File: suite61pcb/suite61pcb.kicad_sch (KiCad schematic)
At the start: 79 parts, among them J1 FFC_Receiver, J2 Joystick_FFC, J3 Battery JST, J4 OLED, SW1 MX_SW_HS, SW10 MX_SW_HS, SW11 MX_SW_HS, SW12 MX_SW_HS, SW13 MX_SW_HS, SW14 MX_SW_HS, SW15 MX_SW_HS, SW16 MX_SW_HS, SW17 MX_SW_HS, SW18 MX_SW_HS, SW19 MX_SW_HS, SW2 MX_SW_HS, SW20 MX_SW_HS, SW21 MX_SW_HS, SW22 MX_SW_HS, SW23 MX_SW_HS, SW24 MX_SW_HS, SW25 MX_SW_HS, SW26 MX_SW_HS, SW27 MX_SW_HS, SW28 MX_SW_HS, SW29 RotaryEncoder_Switch, SW3 MX_SW_HS, SW30 Reset_Button, SW4 MX_SW_HS, SW5 MX_SW_HS, SW6 MX_SW_HS, SW7 MX_SW_HS, SW8 MX_SW_HS, SW9 MX_SW_HS, U1 nice_nano

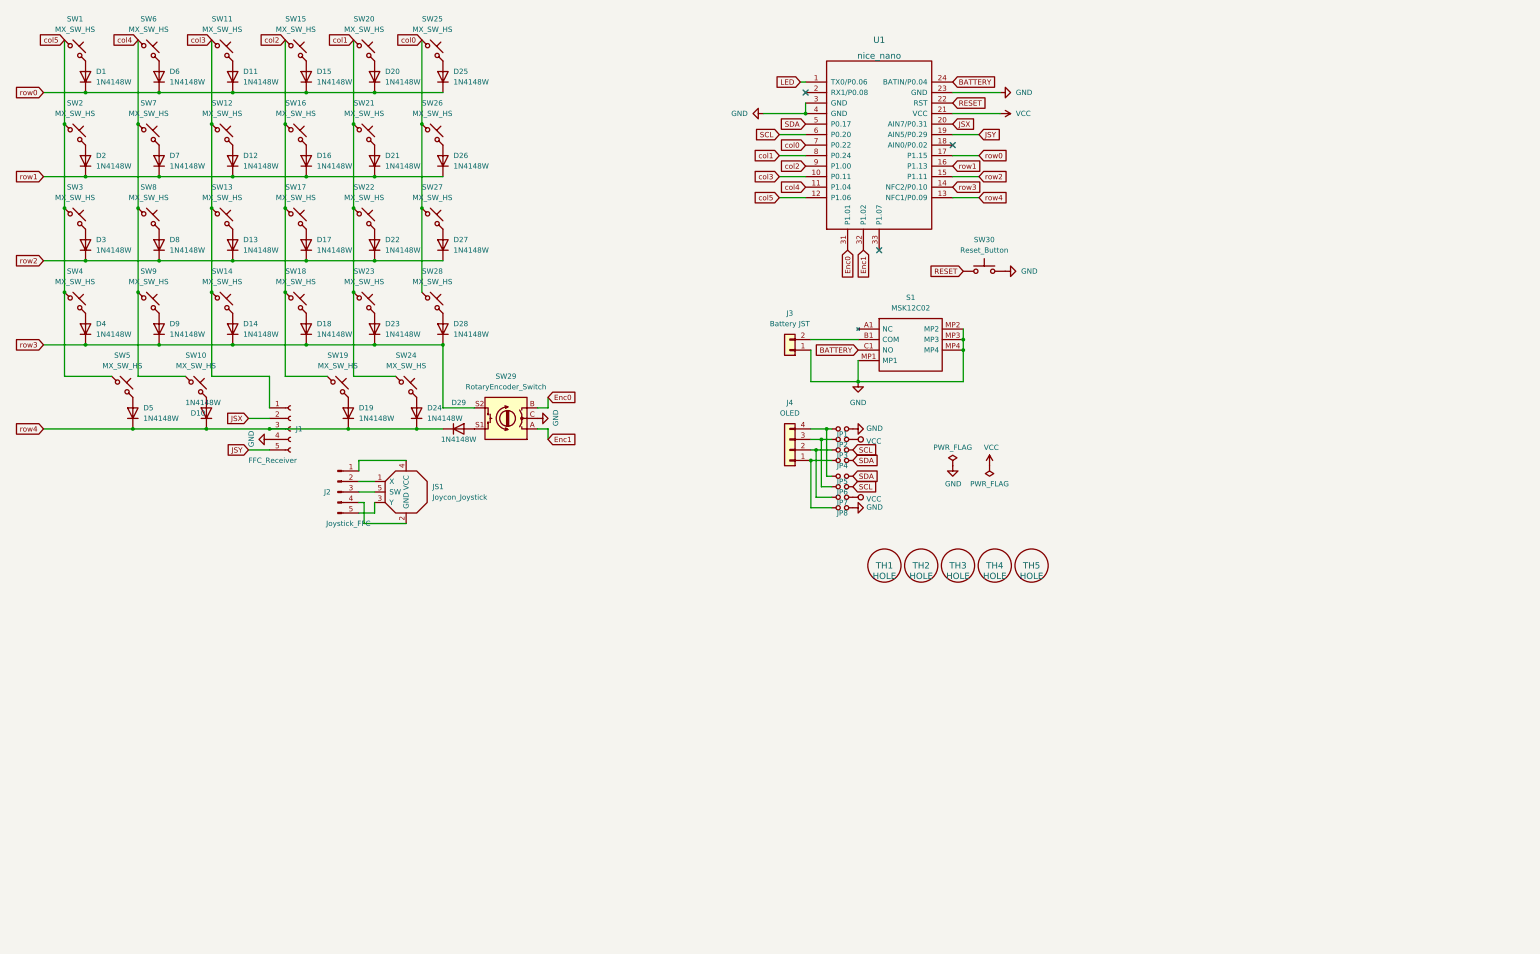
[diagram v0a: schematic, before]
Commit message: Update matrix to 6x6
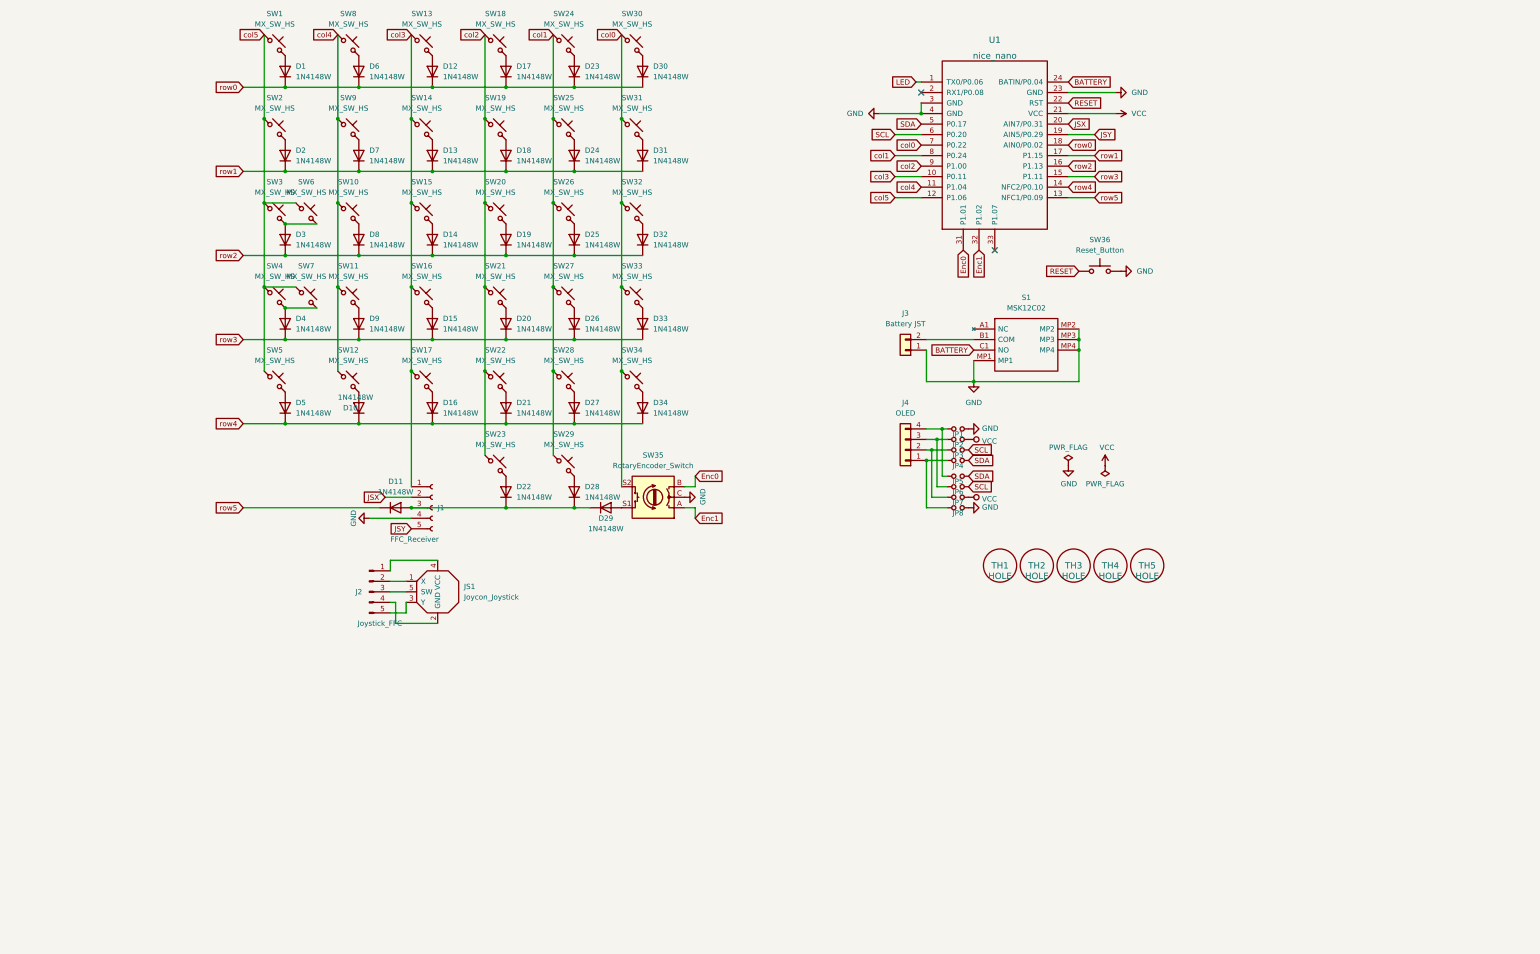
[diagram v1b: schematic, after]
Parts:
- added D11, D16, D22, D28, D34: 1N4148W, Diode_SMD:D_SOD-123, symbol Diode:1N4148W
- added SW17, SW23, SW29, SW34, SW6, SW7: MX_SW_HS, marbastlib-mx:SW_MX_HS_1u, symbol marbastlib-mx:MX_SW_HS
- renumbered D11 to D12, D12 to D13, D13 to D14, D14 to D15, D15 to D17, D16 to D18, D17 to D19, D18 to D20, D19 to D21, D20 to D23, D21 to D24, D22 to D25, D23 to D26, D24 to D27, D25 to D30, D26 to D31, D27 to D32, D28 to D33, SW8 to SW10, SW9 to SW11, SW10 to SW12, SW11 to SW13, SW12 to SW14, SW13 to SW15, SW14 to SW16, SW15 to SW18, SW16 to SW19, SW17 to SW20, SW18 to SW21, SW19 to SW22, SW20 to SW24, SW21 to SW25, SW22 to SW26, SW23 to SW27, SW24 to SW28, SW25 to SW30, SW26 to SW31, SW27 to SW32, SW28 to SW33, SW29 to SW35, SW30 to SW36, SW6 to SW8, SW7 to SW9
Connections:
- net col0: now also SW35.S2, SW34.1
- net col1: now also SW29.1
- net col2: now also SW23.1
- net col3: now also SW17.1
- net col5: now also SW6.1, SW7.1
- net row0: now also U1.18 (AIN0/P0.02); no longer U1.17 (P1.15)
- net row1: now also U1.17 (P1.15); no longer U1.16 (P1.13)
- net row2: now also U1.16 (P1.13); no longer U1.15 (P1.11)
- net row3: now also U1.15 (P1.11); no longer SW35.S2, U1.14 (NFC2/P0.10)
- net row4: now also U1.14 (NFC2/P0.10), D16.1 (K), D34.1 (K); no longer D29.1 (K), J1.3 (Pin_3), U1.13 (NFC1/P0.09)
- net at D3.2 (A), SW3.2: now also SW6.2
- net at D4.2 (A), SW4.2: now also SW7.2
- new net: D11.2 (A), D22.1 (K), D28.1 (K), D29.1 (K), J1.3 (Pin_3)
- new net: D34.2 (A), SW34.2
- new net: D16.2 (A), SW17.2
- new net: D28.2 (A), SW29.2
- new net: D22.2 (A), SW23.2
- new net row5: D11.1 (K), U1.13 (NFC1/P0.09)
- no-connect marks 3 -> 2
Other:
- moved on the sheet: D1, D10, D12, D13, D14, D15, D17, D18, D19, D2, D20, D21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

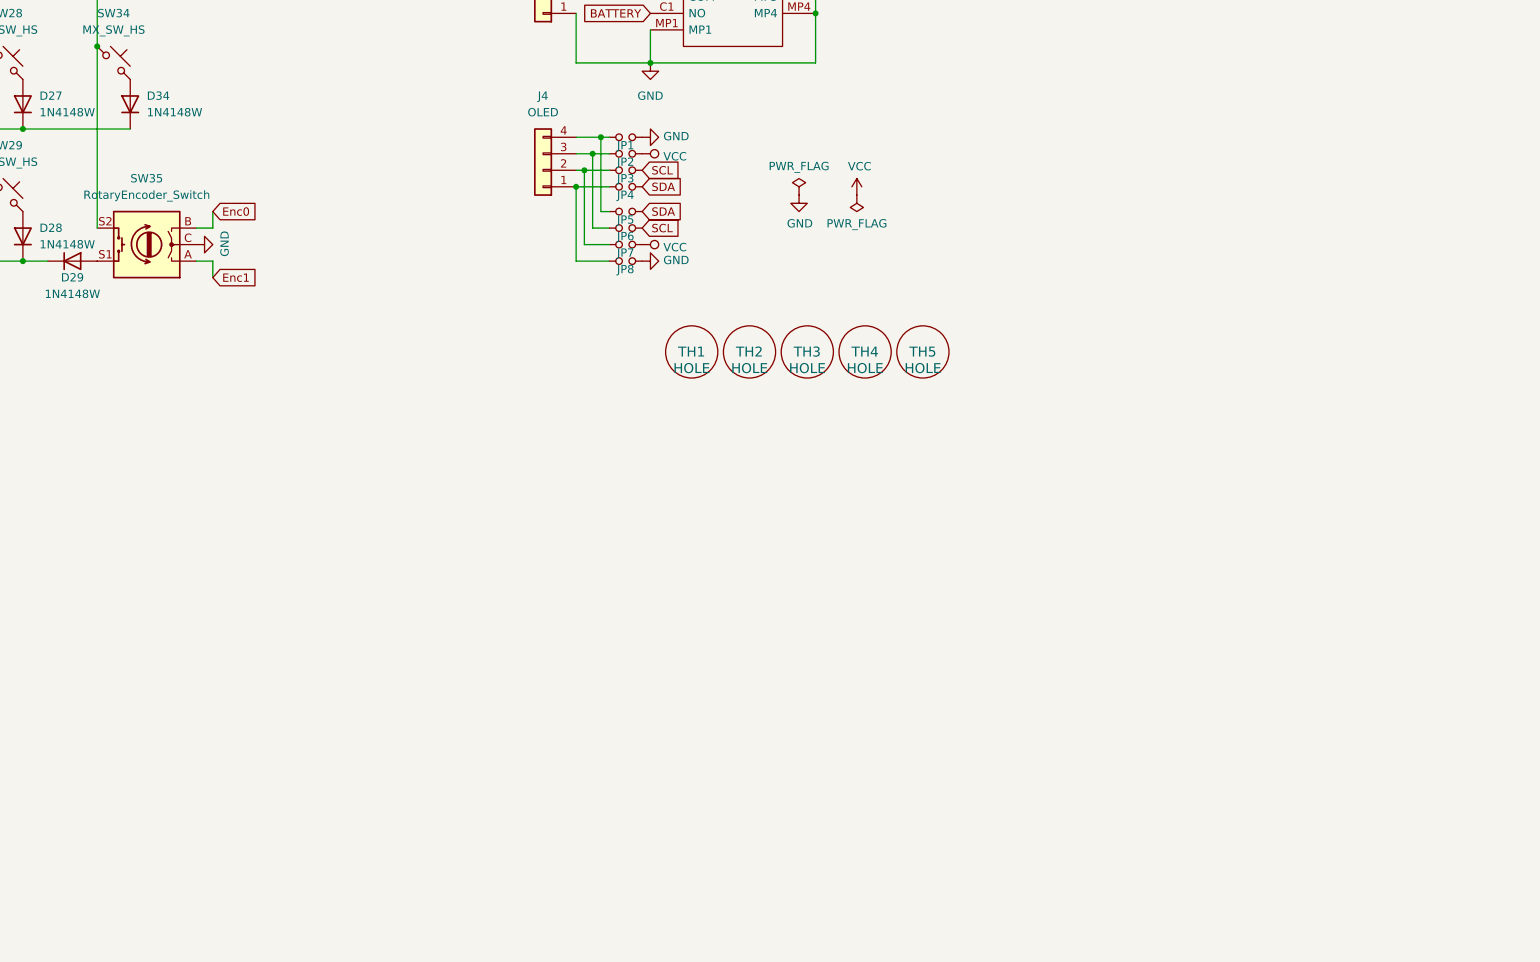
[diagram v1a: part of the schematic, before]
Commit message: create led underglow schematic, upload shield matrix KLE json
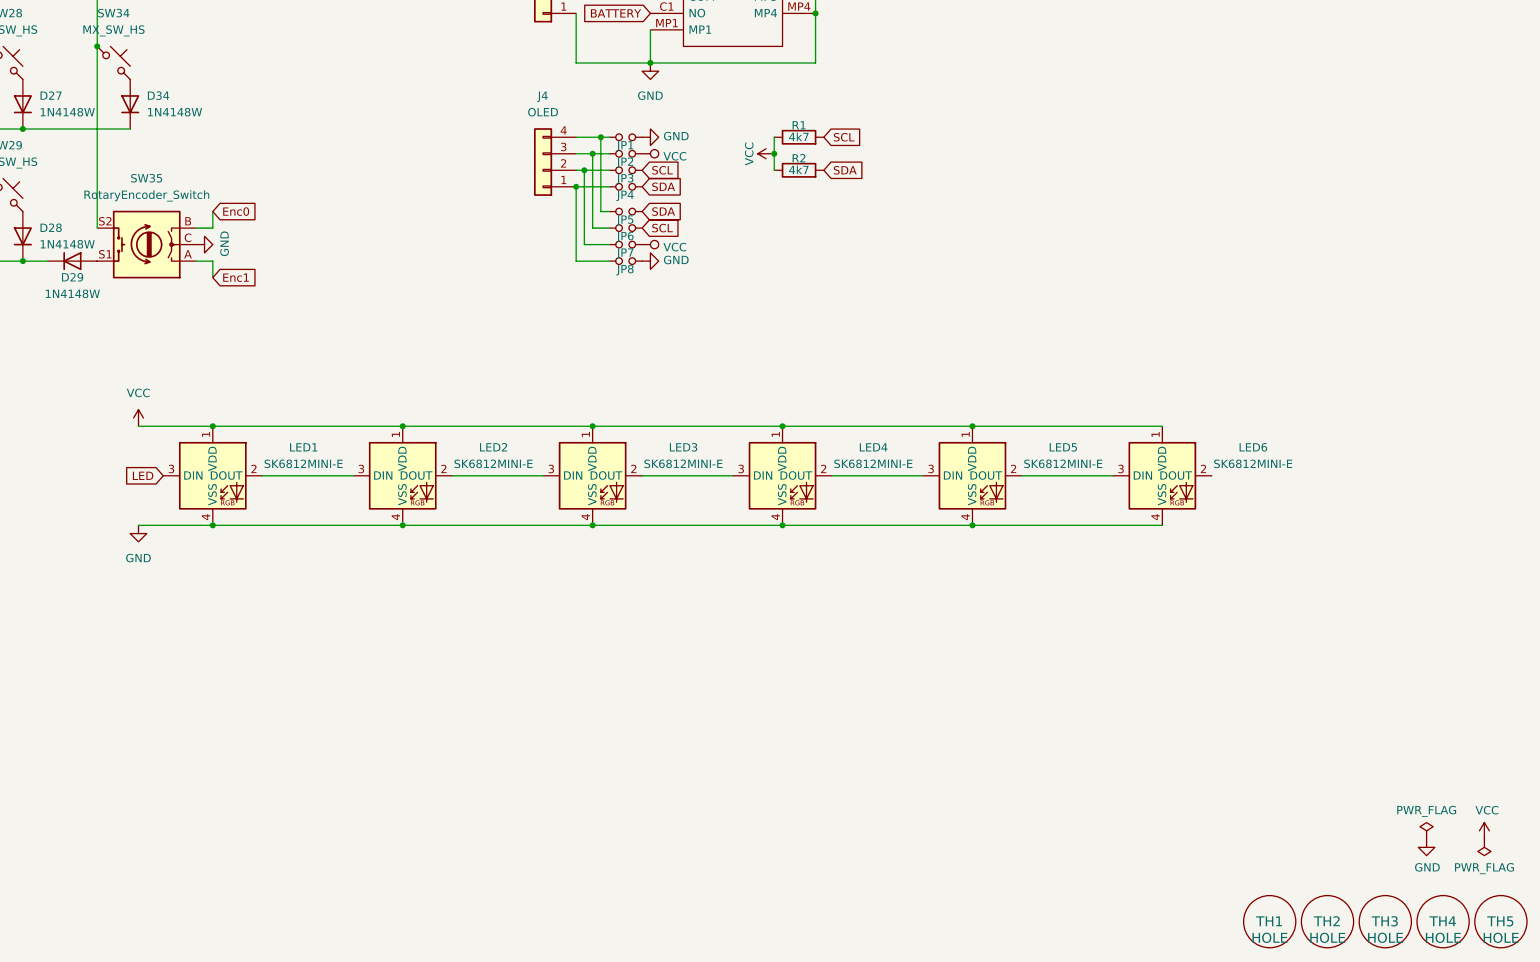
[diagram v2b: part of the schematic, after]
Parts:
- added LED1, LED2, LED3, LED4, LED5, LED6: SK6812MINI-E, marbastlib-various:LED_6028R, symbol marbastlib-various:SK6812MINI-E
- added R1, R2: 4k7, Resistor_THT:R_Axial_DIN0207_L6.3mm_D2.5mm_P7.62mm_Horizontal, symbol Device:R
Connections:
- net GND: now also LED1.4 (VSS), LED2.4 (VSS), LED3.4 (VSS), LED4.4 (VSS), LED5.4 (VSS), LED6.4 (VSS)
- net LED: now also LED1.3 (DIN)
- net SCL: now also R1.2
- net SDA: now also R2.2
- net VCC: now also LED1.1 (VDD), LED2.1 (VDD), LED3.1 (VDD), LED4.1 (VDD), LED5.1 (VDD), LED6.1 (VDD), R1.1, R2.1
- new net: LED2.2 (DOUT), LED3.3 (DIN)
- new net: LED1.2 (DOUT), LED2.3 (DIN)
- new net: LED5.2 (DOUT), LED6.3 (DIN)
- new net: LED4.2 (DOUT), LED5.3 (DIN)
- new net: LED3.2 (DOUT), LED4.3 (DIN)
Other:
- moved on the sheet: TH1, TH2, TH3, TH4, TH5

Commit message: create .pcb
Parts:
- JP1, JP2, JP3, JP4, JP5, JP6, JP7, JP8: footprint SofleKeyboard-footprint:Jumper -> suite61:jumper
- JS1: footprint marbastlib-various:joystick_psp1000 -> suite61:2-way joystick switch
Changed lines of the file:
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@@
       (effects (font (size 1.27 1.27)) hide)
     )
-    (property "Footprint" "SofleKeyboard-footprint:Jumper" (id 2) (at 251.46 120.65 0)
+    (property "Footprint" "suite61:jumper" (id 2) (at 251.46 120.65 0)
       (effects (font (size 1.27 1.27)) hide)
     )
@@
       (effects (font (size 1.27 1.27)) hide)
     )
-    (property "Footprint" "SofleKeyboard-footprint:Jumper" (id 2) (at 251.46 139.7 0)
+    (property "Footprint" "suite61:jumper" (id 2) (at 251.46 139.7 0)
       (effects (font (size 1.27 1.27)) hide)
     )
@@
       (effects (font (size 1.27 1.27)) hide)
     )
-    (property "Footprint" "SofleKeyboard-footprint:Jumper" (id 2) (at 251.46 137.16 0)
+    (property "Footprint" "suite61:jumper" (id 2) (at 251.46 137.16 0)
       (effects (font (size 1.27 1.27)) hide)
     )
@@
       (effects (font (size 1.27 1.27)) hide)
     )
-    (property "Footprint" "SofleKeyboard-footprint:Jumper" (id 2) (at 251.46 128.27 0)
+    (property "Footprint" "suite61:jumper" (id 2) (at 251.46 128.27 0)
       (effects (font (size 1.27 1.27)) hide)
     )
@@
       (effects (font (size 1.27 1.27)) (justify left))
     )
-    (property "Footprint" "marbastlib-various:joystick_psp1000" (id 2) (at 125.73 160.02 0)
+    (property "Footprint" "suite61:2-way joystick switch" (id 2) (at 125.73 160.02 0)
       (effects (font (size 1.27 1.27)) hide)
     )
@@
       (effects (font (size 1.27 1.27)) hide)
     )
-    (property "Footprint" "SofleKeyboard-footprint:Jumper" (id 2) (at 251.46 123.19 0)
+    (property "Footprint" "suite61:jumper" (id 2) (at 251.46 123.19 0)
       (effects (font (size 1.27 1.27)) hide)
     )
@@
       (effects (font (size 1.27 1.27)) hide)
     )
-    (property "Footprint" "SofleKeyboard-footprint:Jumper" (id 2) (at 251.46 125.73 0)
+    (property "Footprint" "suite61:jumper" (id 2) (at 251.46 125.73 0)
       (effects (font (size 1.27 1.27)) hide)
     )
@@
       (effects (font (size 1.27 1.27)) hide)
     )
-    (property "Footprint" "SofleKeyboard-footprint:Jumper" (id 2) (at 251.46 132.08 0)
+    (property "Footprint" "suite61:jumper" (id 2) (at 251.46 132.08 0)
       (effects (font (size 1.27 1.27)) hide)
     )
@@
       (effects (font (size 1.27 1.27)) hide)
     )
-    (property "Footprint" "SofleKeyboard-footprint:Jumper" (id 2) (at 251.46 134.62 0)
+    (property "Footprint" "suite61:jumper" (id 2) (at 251.46 134.62 0)
       (effects (font (size 1.27 1.27)) hide)
     )
@@
     )
     (path "/0517f743-12bb-45a2-a811-d212212c6032"
-      (reference "JP1") (unit 1) (value "Jumper_NO_Small") (footprint "SofleKeyboard-footprint:Jumper")
+      (reference "JP1") (unit 1) (value "Jumper_NO_Small") (footprint "suite61:jumper")
     )
     (path "/b454ce70-3feb-4d4a-8a73-aa3622809df8"
-      (reference "JP2") (unit 1) (value "Jumper_NO_Small") (footprint "SofleKeyboard-footprint:Jumper")
+      (reference "JP2") (unit 1) (value "Jumper_NO_Small") (footprint "suite61:jumper")
     )
     (path "/cb5c3395-1cef-4d8e-9f50-156870cc1ea9"
-      (reference "JP3") (unit 1) (value "Jumper_NO_Small") (footprint "SofleKeyboard-footprint:Jumper")
+      (reference "JP3") (unit 1) (value "Jumper_NO_Small") (footprint "suite61:jumper")
     )
     (path "/3aa5de58-1ae6-4a0e-ad8f-ef496c9626dd"
-      (reference "JP4") (unit 1) (value "Jumper_NO_Small") (footprint "SofleKeyboard-footprint:Jumper")
+      (reference "JP4") (unit 1) (value "Jumper_NO_Small") (footprint "suite61:jumper")
     )
     (path "/d13ca184-63c3-4f14-a962-6f049351637b"
-      (reference "JP5") (unit 1) (value "Jumper_NO_Small") (footprint "SofleKeyboard-footprint:Jumper")
+      (reference "JP5") (unit 1) (value "Jumper_NO_Small") (footprint "suite61:jumper")
     )
     (path "/d8d57651-6fb9-424c-af4b-b7cb1d2d9785"
-      (reference "JP6") (unit 1) (value "Jumper_NO_Small") (footprint "SofleKeyboard-footprint:Jumper")
+      (reference "JP6") (unit 1) (value "Jumper_NO_Small") (footprint "suite61:jumper")
     )
     (path "/334e7cbc-dda8-4471-b3b3-d9d173ec4c0d"
-      (reference "JP7") (unit 1) (value "Jumper_NO_Small") (footprint "SofleKeyboard-footprint:Jumper")
+      (reference "JP7") (unit 1) (value "Jumper_NO_Small") (footprint "suite61:jumper")
     )
     (path "/291e1b9f-5e70-4582-9f78-463f20cf6648"
-      (reference "JP8") (unit 1) (value "Jumper_NO_Small") (footprint "SofleKeyboard-footprint:Jumper")
+      (reference "JP8") (unit 1) (value "Jumper_NO_Small") (footprint "suite61:jumper")
     )
     (path "/59f3f8c3-a02a-45e6-b943-5a967aac25b3"
-      (reference "JS1") (unit 1) (value "Joycon_Joystick") (footprint "marbastlib-various:joystick_psp1000")
+      (reference "JS1") (unit 1) (value "Joycon_Joystick") (footprint "suite61:2-way joystick switch")
     )
     (path "/a149b419-122d-4faa-866a-fc943963345c"
